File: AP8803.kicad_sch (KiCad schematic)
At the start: 14 parts, among them U1 AL8803_SIMETRIX

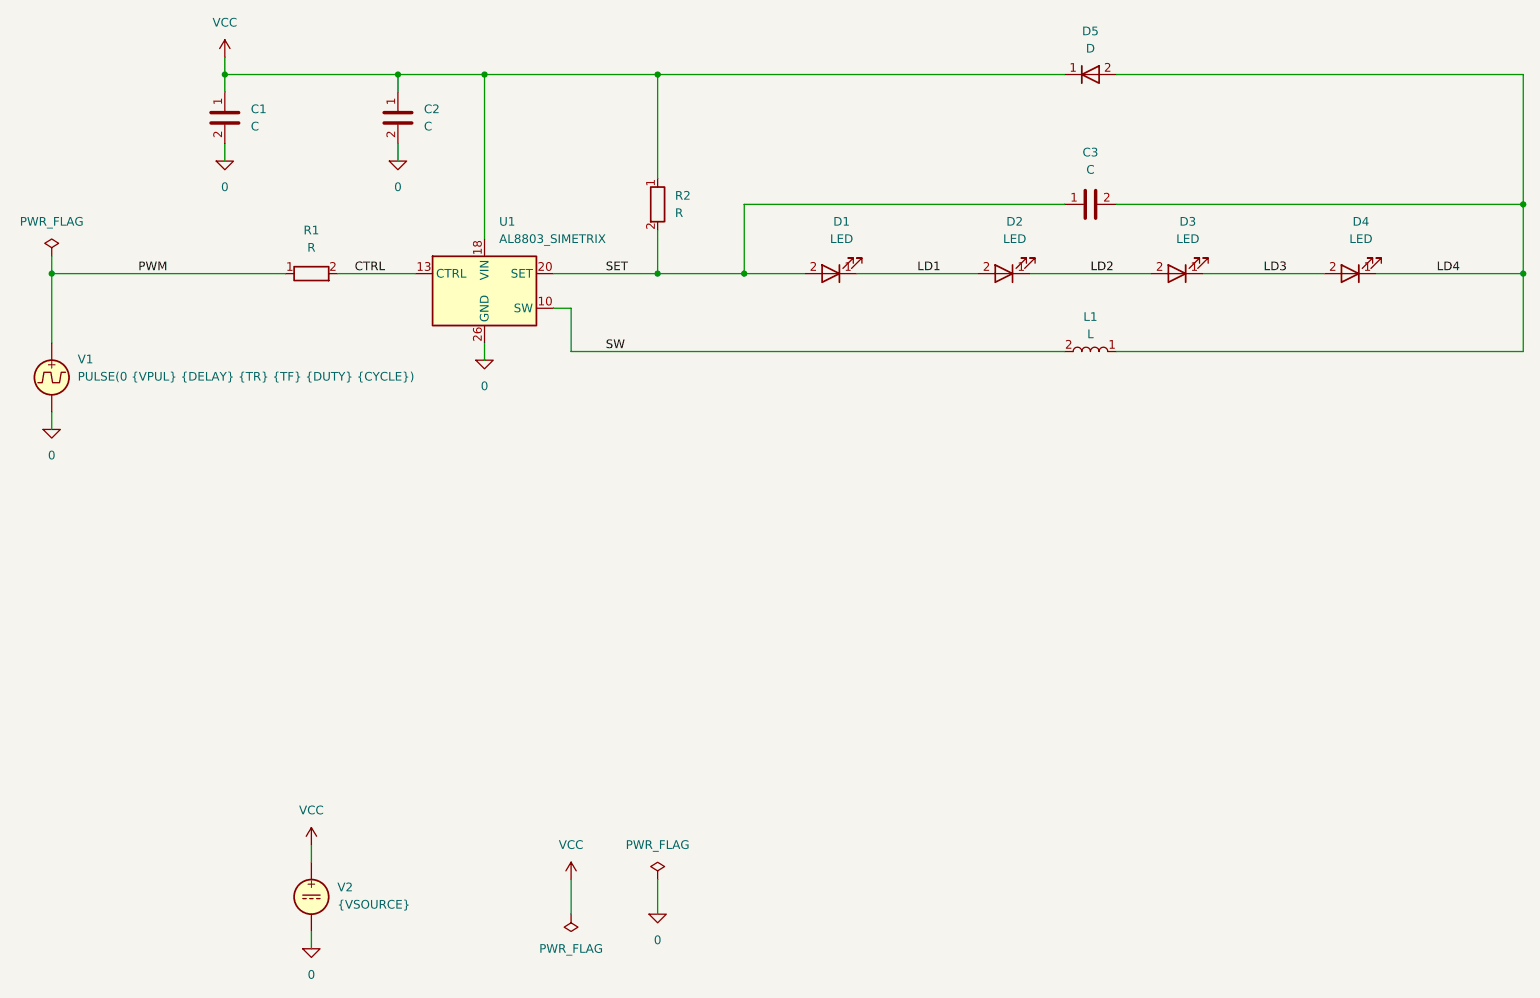
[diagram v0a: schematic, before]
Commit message: Add files via upload
LTspice simulation files
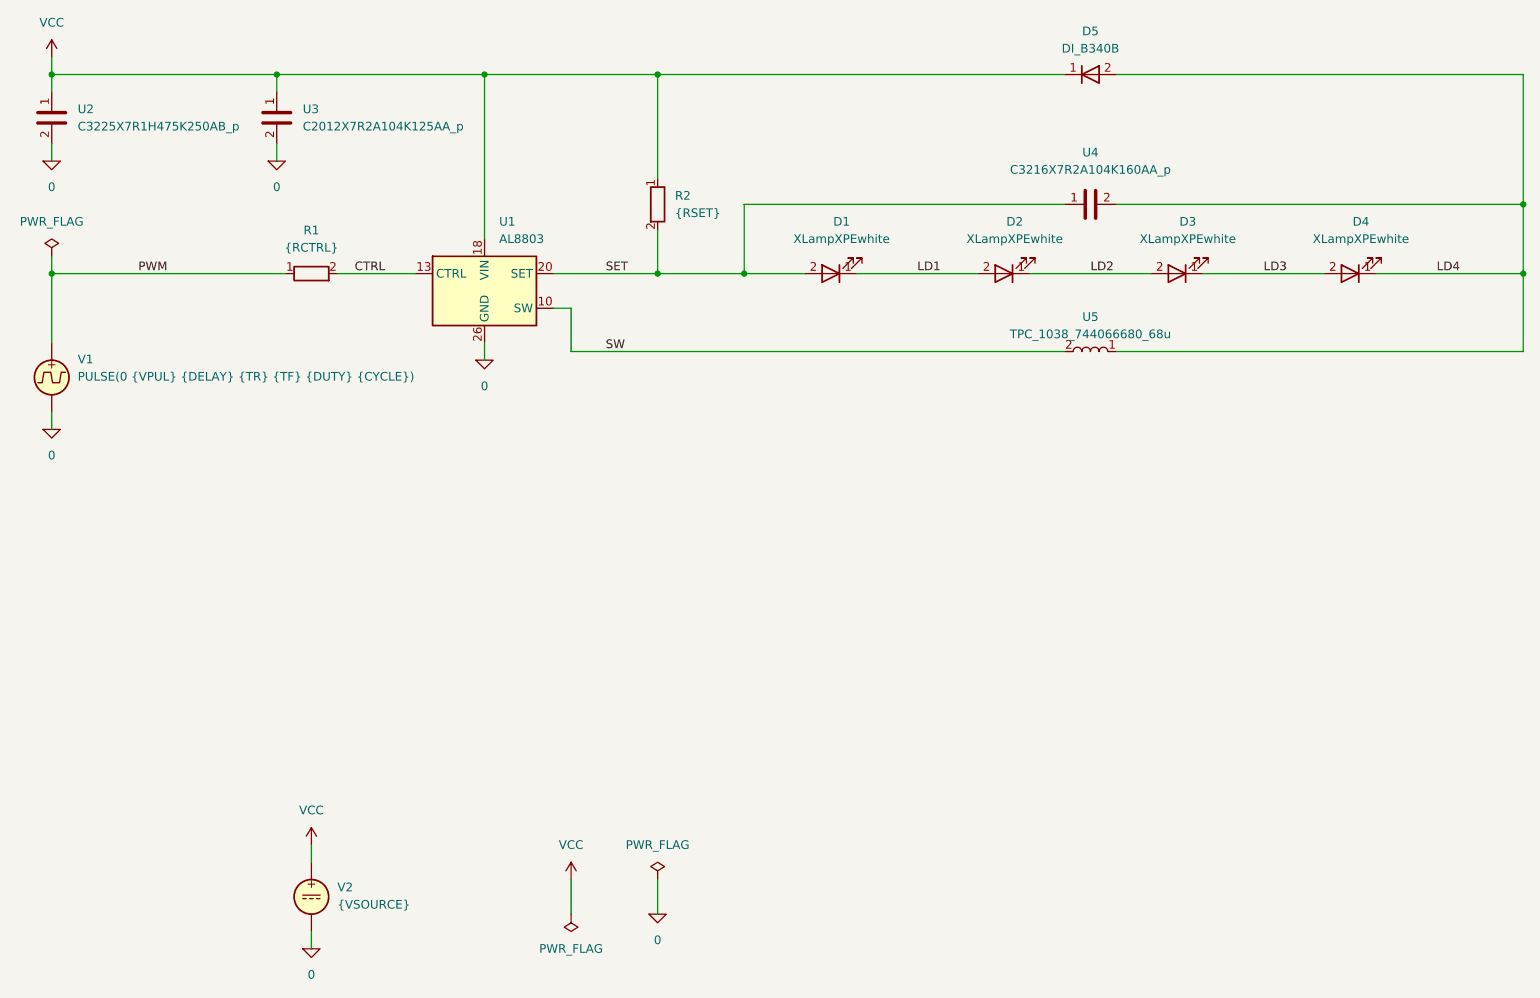
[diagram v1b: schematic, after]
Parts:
- removed C2, C3: C, symbol AP8803:C
- added U3: C2012X7R2A104K125AA_p, symbol AP8803:C
- added U4: C3216X7R2A104K160AA_p, symbol AP8803:C
- D1, D2, D3, D4: value LED -> XLampXPEwhite
- D5: value D -> DI_B340B
- R1: value R -> {RCTRL}
- R2: value R -> {RSET}
- U1: value AL8803_SIMETRIX -> AL8803
- U2: renamed from C1; value C -> C3225X7R1H475K250AB_p
- U5: renamed from L1; value L -> TPC_1038_744066680_68u
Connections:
- net 0: now also U3.2
- net LD4: now also U4.2
- net SET: now also U4.1
- net VCC: now also U3.1
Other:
- title: (none) -> 30V 1A BUCK LED DRIVER
- moved on the sheet: U2
